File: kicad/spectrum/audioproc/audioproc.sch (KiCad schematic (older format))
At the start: 5 parts

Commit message: Schematics update
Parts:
- added J?: ROT, symbol Connector_Generic:Conn_01x03
- added J?: CONTROL, Connector_JST:JST_EH_B4B-EH-A_1x04_P2.50mm_Vertical, symbol Connector_Generic:Conn_01x04
- added J?: AUDIO, symbol Connector_Generic:Conn_01x03
- added J?: FP_POWER, Connector_JST:JST_EH_B4B-EH-A_1x04_P2.50mm_Vertical, symbol Connector_Generic:Conn_01x04
- added U?: L78L12_TO92, Package_TO_SOT_THT:TO-92_Inline, symbol Regulator_Linear:L78L12_TO92
- added U?: LM7805_TO220, Package_TO_SOT_THT:TO-220-3_Vertical, symbol Regulator_Linear:LM7805_TO220
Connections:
- net labels added: +5V, MUTE, OUT_L, OUT_R, REMOTE, ROT-A, ROT-B, SP_L, SP_R, STBY
- wire segments 26 -> 72
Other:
- moved on the sheet: J?, U?

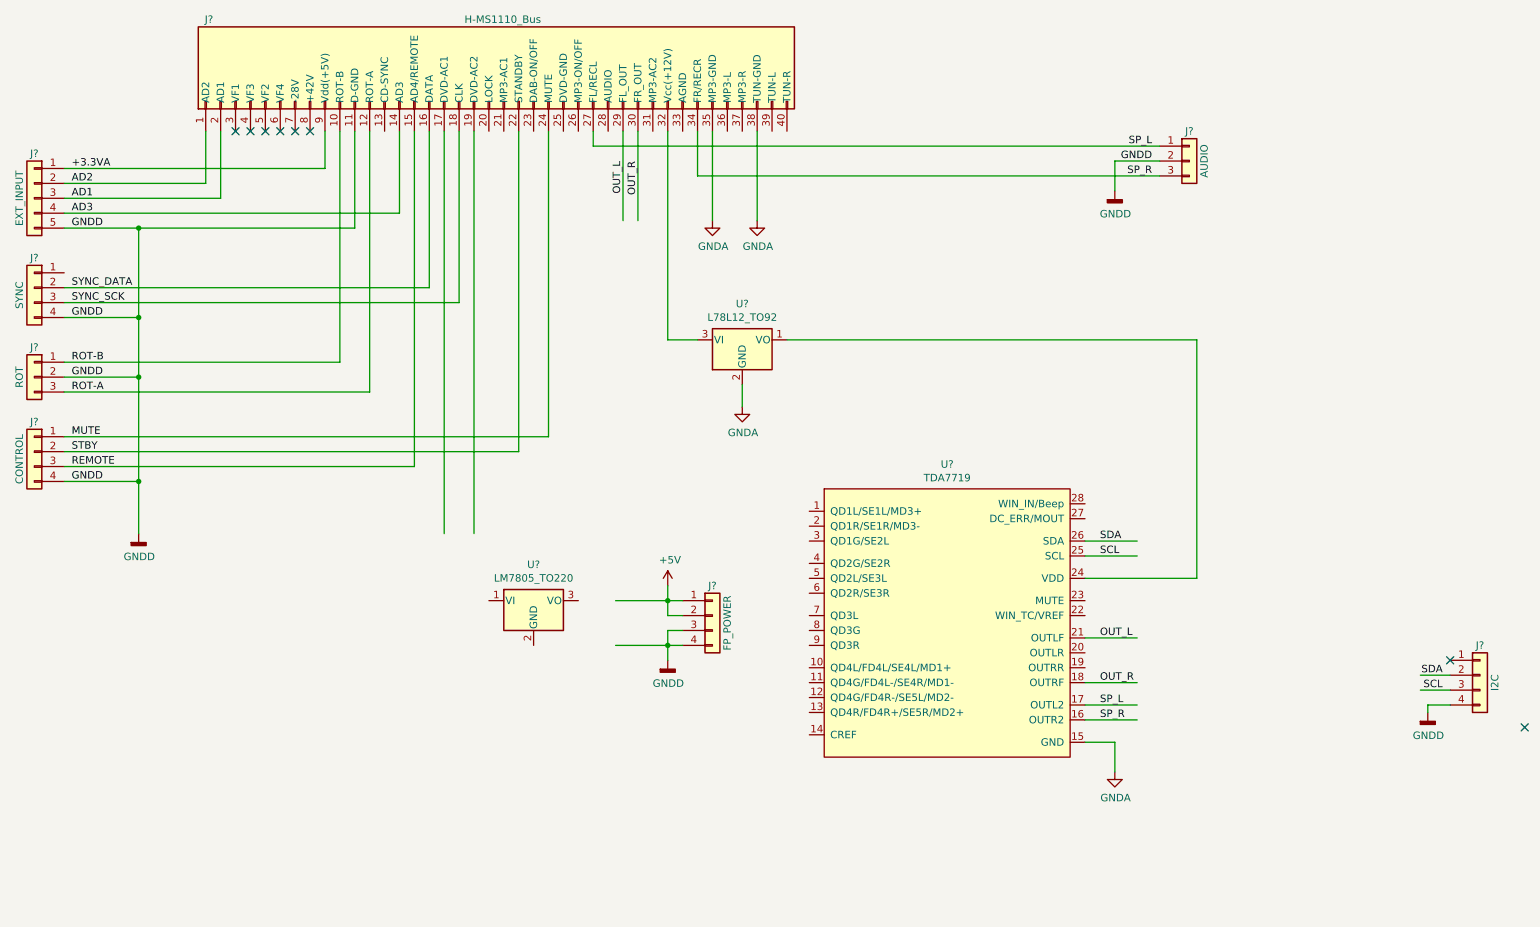
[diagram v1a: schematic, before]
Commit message: Audioproc schematic update
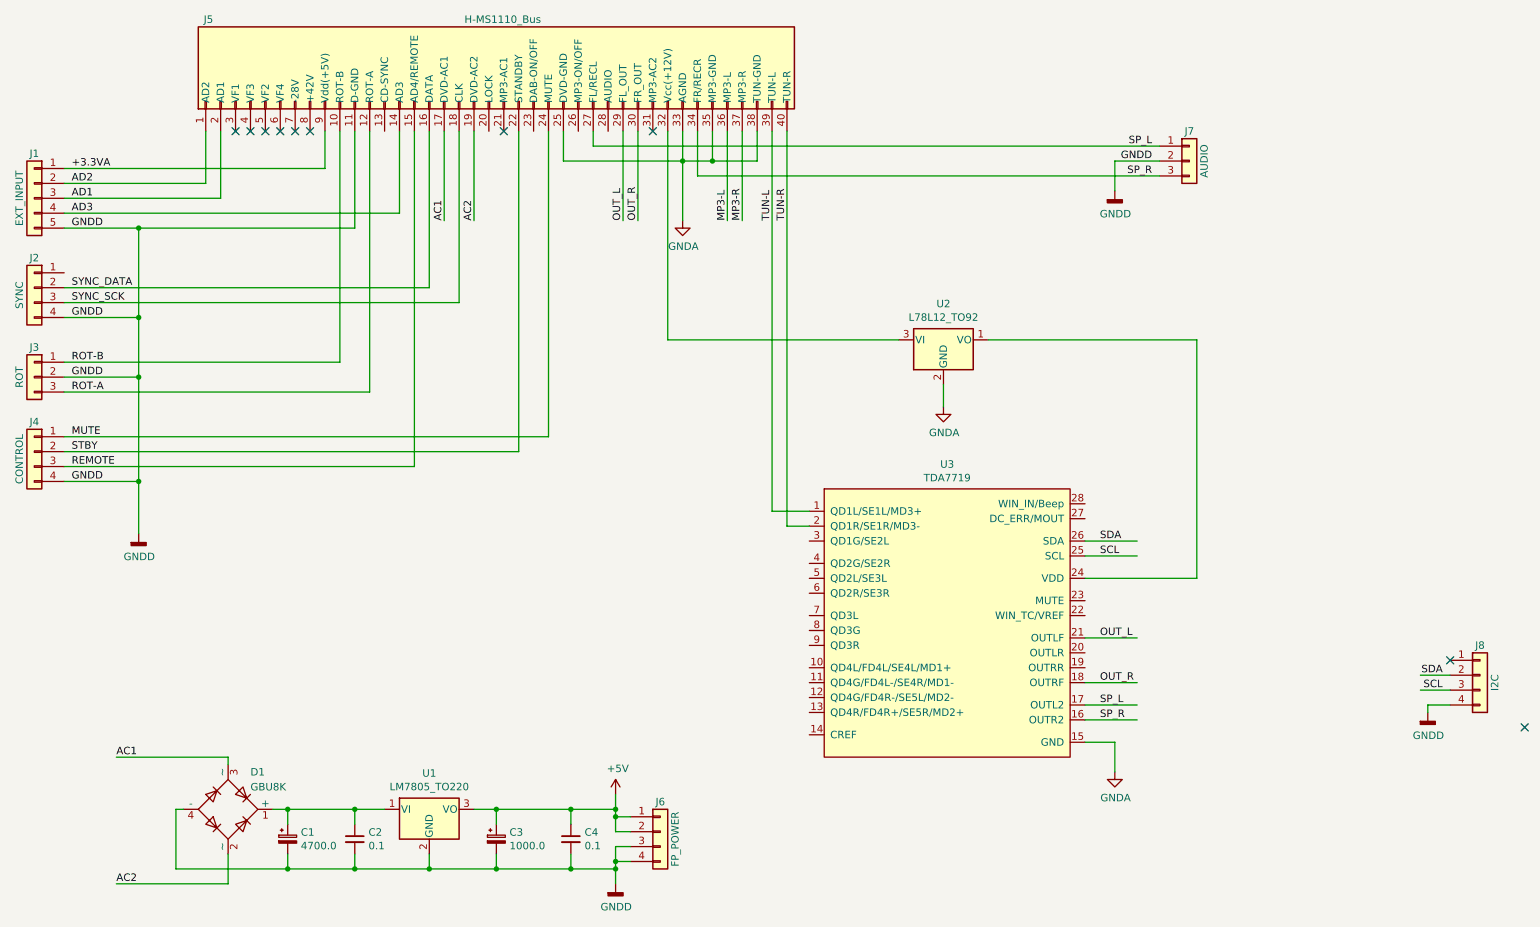
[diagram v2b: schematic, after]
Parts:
- added C1: 4700.0, Capacitor_THT:CP_Radial_D10.0mm_P5.00mm_P7.50mm, symbol Device:CP_Small
- added C2, C4: 0.1, Capacitor_THT:C_Rect_L7.0mm_W3.5mm_P5.00mm, symbol Device:C_Small
- added C3: 1000.0, Capacitor_THT:CP_Radial_D10.0mm_P5.00mm, symbol Device:CP_Small
- added D1: GBU8K, Diode_THT:Diode_Bridge_Vishay_GBU, symbol Diode_Bridge:GBU8K
- J1: renamed from J?; footprint (none) -> Connector_JST:JST_EH_B5B-EH-A_1x05_P2.50mm_Vertical
- J3, J7: renamed from J?; footprint (none) -> Connector_JST:JST_EH_B3B-EH-A_1x03_P2.50mm_Vertical
- gave numbers to parts that had none: 8
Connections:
- net labels added: AC1, AC2, MP3-L, MP3-R, TUN-L, TUN-R
- wire segments 72 -> 111
- no-connect marks 8 -> 10
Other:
- moved on the sheet: J6, U1, U2
